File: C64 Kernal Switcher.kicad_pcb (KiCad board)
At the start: 2 copper layers, 8 parts, among them J1 LED, J2 Signals, U1 2364, U2 28C256

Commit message: PCB layed out, need measuring
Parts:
- added A1: Arduino_Nano_v3.x, Modules:Arduino_Nano, F.Cu at (66.0, 109.9)
- added J3: Power, Pin_Headers:Pin_Header_Straight_1x02_Pitch2.54mm, F.Cu at (66.0, 113.0)
- moved JP1 97.0 mm to (66.0, 54.0), turned to 90 degrees
- moved JP2 88.5 mm to (76.2, 54.0), turned to 90 degrees
- moved R1 77.4 mm to (71.1, 104.8)
- moved J1 75.3 mm to (73.7, 113.0), turned to 90 degrees
- moved R2 64.7 mm to (83.8, 104.8)
- moved J2 62.7 mm to (86.4, 113.0), turned to 90 degrees
- moved U1 0.63 mm to (69.2, 62.9)
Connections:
- J2 pad 1: (no net) -> ESXROM
- J2 pad 2: (no net) -> RESET
- J2 pad 3: (no net) -> RESTORE
- R1 pad 2: (no net) -> LED1
- R2 pad 2: (no net) -> LED2
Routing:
- net VCC: track 0.00 -> 92.1 mm
- net A13: track 0.00 -> 79.6 mm, vias 0 -> 3
- net A14: track 0.00 -> 75.2 mm, vias 0 -> 2
- net /A12: track 0.00 -> 27.1 mm
- net Net-(A1-Pad27): track 0.00 -> 22.4 mm
- net Net-(J1-Pad3): track 0.00 -> 18.2 mm
- net /A11: track 0.00 -> 16.9 mm
- net /CS: track 0.00 -> 11.3 mm
- net Net-(J1-Pad1): track 0.00 -> 9.31 mm
- net ESXROM: track 0.00 -> 8.94 mm
- net LED2: track 0.00 -> 5.08 mm
- net LED1: track 0.00 -> 5.08 mm
- net RESTORE: track 0.00 -> 3.81 mm
- net RESET: track 0.00 -> 3.81 mm
- net /D7: track 0.00 -> 3.17 mm
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- added copper zone on B.Cu, net GND
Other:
- board outline added: 38.1 x 61.6 mm

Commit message: Layout redone
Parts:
- removed A1: Arduino_Nano_v3.x, Modules:Arduino_Nano
- added C1: 100nF, Capacitors_THT:C_Disc_D4.7mm_W2.5mm_P5.00mm, F.Cu at (69.8, 66.0)
- added R3: 560, Resistors_THT:R_Axial_DIN0207_L6.3mm_D2.5mm_P10.16mm_Horizontal, F.Cu at (82.5, 99.1)
- added U3: 27C256, Housings_DIP:DIP-28_W15.24mm_Socket, F.Cu at (72.4, 68.6)
- J1: value LED -> Signals; footprint Pin_Headers:Pin_Header_Straight_1x03_Pitch2.54mm -> Pin_Headers:Pin_Header_Angled_1x02_Pitch2.54mm
- J2: value Signals -> RGB; footprint Pin_Headers:Pin_Header_Straight_1x03_Pitch2.54mm -> Pin_Headers:Pin_Header_Straight_2x03_Pitch2.54mm
- J3: value Power -> LED; footprint Pin_Headers:Pin_Header_Straight_1x02_Pitch2.54mm -> Pin_Headers:Pin_Header_Angled_1x03_Pitch2.54mm
- R1: value 330 -> 1k
- R2: value 330 -> 3k3
- U1: footprint Housings_DIP:DIP-24_W15.24mm_Socket -> 2364:DIP-24_W15.24mm_Socket
- U2: value 28C256 -> PIC12F629-I/MS; footprint Housings_DIP:DIP-28_W15.24mm_Socket -> Housings_DIP:DIP-8_W7.62mm_Socket; moved to B.Cu
- moved U2 24.7 mm to (82.5, 76.2), turned to 180 degrees
- moved J3 23.1 mm to (87.6, 104.8), turned to 0 degrees
- moved JP1 16.6 mm to (78.1, 65.4), turned to 270 degrees
- moved JP2 12.8 mm to (81.9, 65.4)
- moved U1 10.8 mm to (69.8, 73.7)
- moved J2 10.6 mm to (76.2, 109.9)
- moved R2 7.65 mm to (78.7, 99.1), turned to 90 degrees
- moved R1 6.87 mm to (74.9, 99.1), turned to 90 degrees
- moved J1 4.96 mm to (69.8, 109.9), turned to 180 degrees
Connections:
- J1 pad 1: Net-(J1-Pad1) -> ~RESTORE
- J1 pad 2: GND -> ~RESET
- J2 pad 1: ESXROM -> BLUE
- J2 pad 2: RESET -> GREEN
- J2 pad 3: RESTORE -> GND
- J3 pad 1: VCC -> RED
- J3 pad 2: Net-(A1-Pad27) -> GND
- R1 pad 1: Net-(J1-Pad1) -> BLUE
- R1 pad 2: LED1 -> A14
- R2 pad 1: Net-(J1-Pad3) -> GREEN
- R2 pad 2: LED2 -> A13
- U2 pad 1: A14 -> VCC
- U2 pad 2: /A12 -> A14
- U2 pad 3: /A7 -> A13
- U2 pad 4: /A6 -> ~RESTORE
- U2 pad 5: /A5 -> Net-(R3-Pad2)
- U2 pad 6: /A4 -> ~RESET
- U2 pad 7: /A3 -> (no net)
- U2 pad 8: /A2 -> GND
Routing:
- net VCC: track 92.1 -> 37.9 mm
- net A13: track 79.6 -> 41.5 mm, vias 3 -> 2
- net ~RESTORE: track 0.00 -> 37.6 mm
- net A14: track 75.2 -> 38.6 mm, vias 2 -> 5
- net ~RESET: track 0.00 -> 34.5 mm
- net Net-(A1-Pad27): track 22.4 -> 0.00 mm
- net RED: track 0.00 -> 19.2 mm
- net Net-(J1-Pad3): track 18.2 -> 0.00 mm
- net BLUE: track 0.00 -> 13.5 mm, vias 0 -> 2
- net Net-(R3-Pad2): track 0.00 -> 10.5 mm, vias 0 -> 2
- net GREEN: track 0.00 -> 10.1 mm
- net Net-(J1-Pad1): track 9.31 -> 0.00 mm
- net ESXROM: track 8.94 -> 0.00 mm
- net /CS: track 11.3 -> 3.17 mm
- net /A11: track 16.9 -> 10.8 mm
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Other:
- board size 38.1 x 61.6 mm -> 20.3 x 47.6 mm

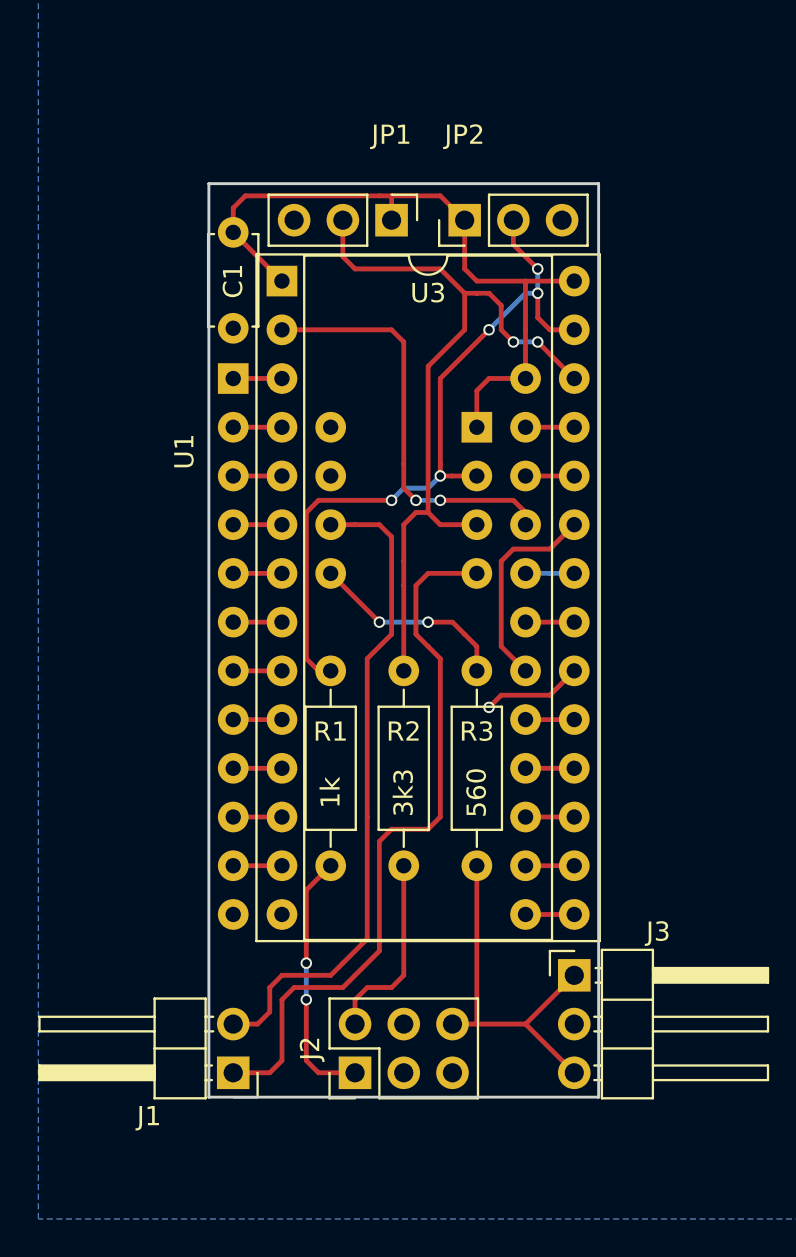
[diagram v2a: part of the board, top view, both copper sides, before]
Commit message: Updated silkscreen
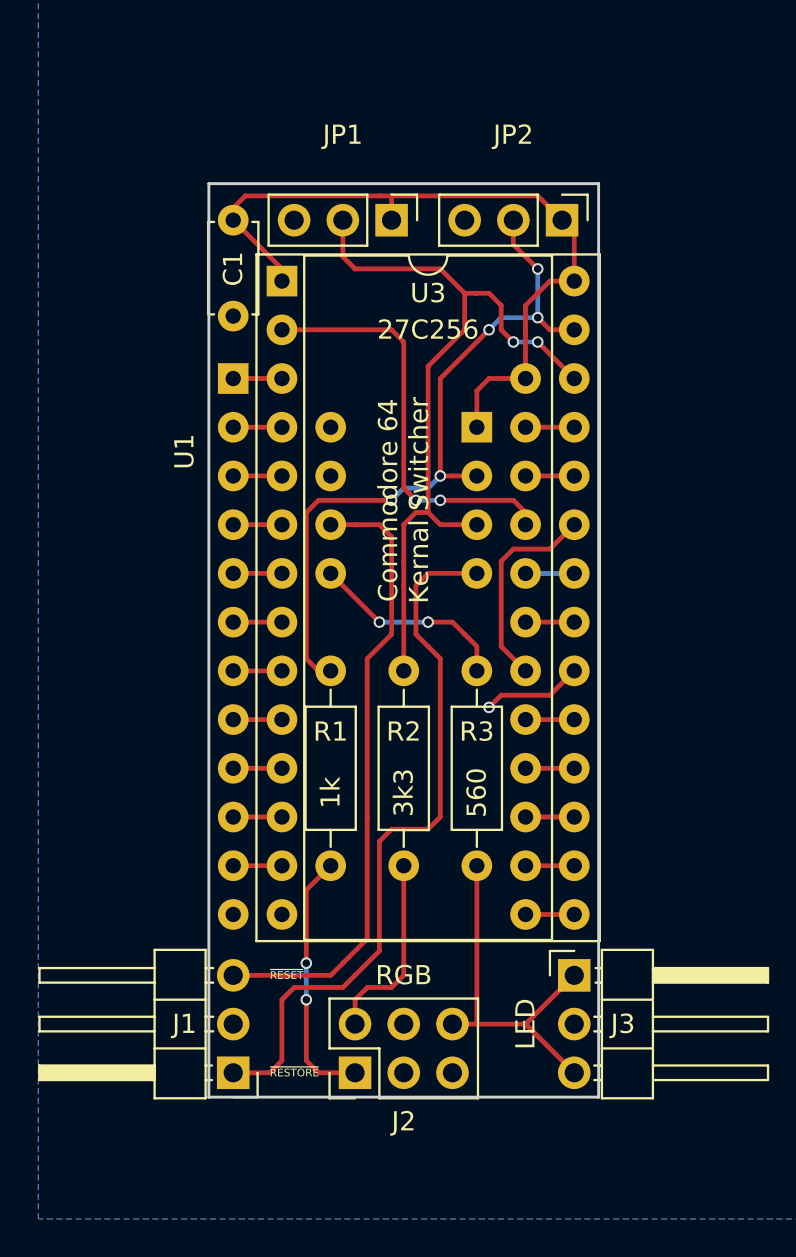
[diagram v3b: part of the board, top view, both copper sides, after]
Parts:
- J1: footprint Pin_Headers:Pin_Header_Angled_1x02_Pitch2.54mm -> Pin_Headers:Pin_Header_Angled_1x03_Pitch2.54mm
- U2: value PIC12F629-I/MS -> PIC12F629
- moved JP2 5.08 mm to (87.0, 65.4), turned to 270 degrees
- moved C1 0.64 mm to (69.8, 65.4)
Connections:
- J1 pad 2: ~RESET -> (no net)
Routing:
- net ~RESET: track 34.5 -> 32.7 mm
- net VCC: track 37.9 -> 39.7 mm
- net A14: track 38.6 -> 38.1 mm
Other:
- board text added: "A13"
- board text added: "A14"
- board text added: "B"
- board text added: "Commodore 64 Kernal Switcher"
- board text added: "Commodore 64 Quad Kernal Revision A"
- board text added: "G"
- board text added: "GND"
- board text added: "LED"
- board text added: "R"
- board text added: "RGB"
- board text added: "~RESET"
- board text added: "~RESTORE"
